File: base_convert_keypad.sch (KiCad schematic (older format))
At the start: 32 parts, among them SW10 B13, SW11 B2, SW12 B6, SW13 B10, SW14 B14, SW15 B3, SW16 B7, SW17 B11, SW18 B15, SW19 0, SW20 4, SW21 8, SW22 C, SW23 1, SW24 5, SW25 9, SW26 D, SW27 2, SW28 6, SW29 A, SW3 B0, SW30 E, SW31 3, SW32 7, SW33 B, SW34 F, SW4 B4, SW5 B8, SW6 B12, SW7 B1, SW8 B5, SW9 B9

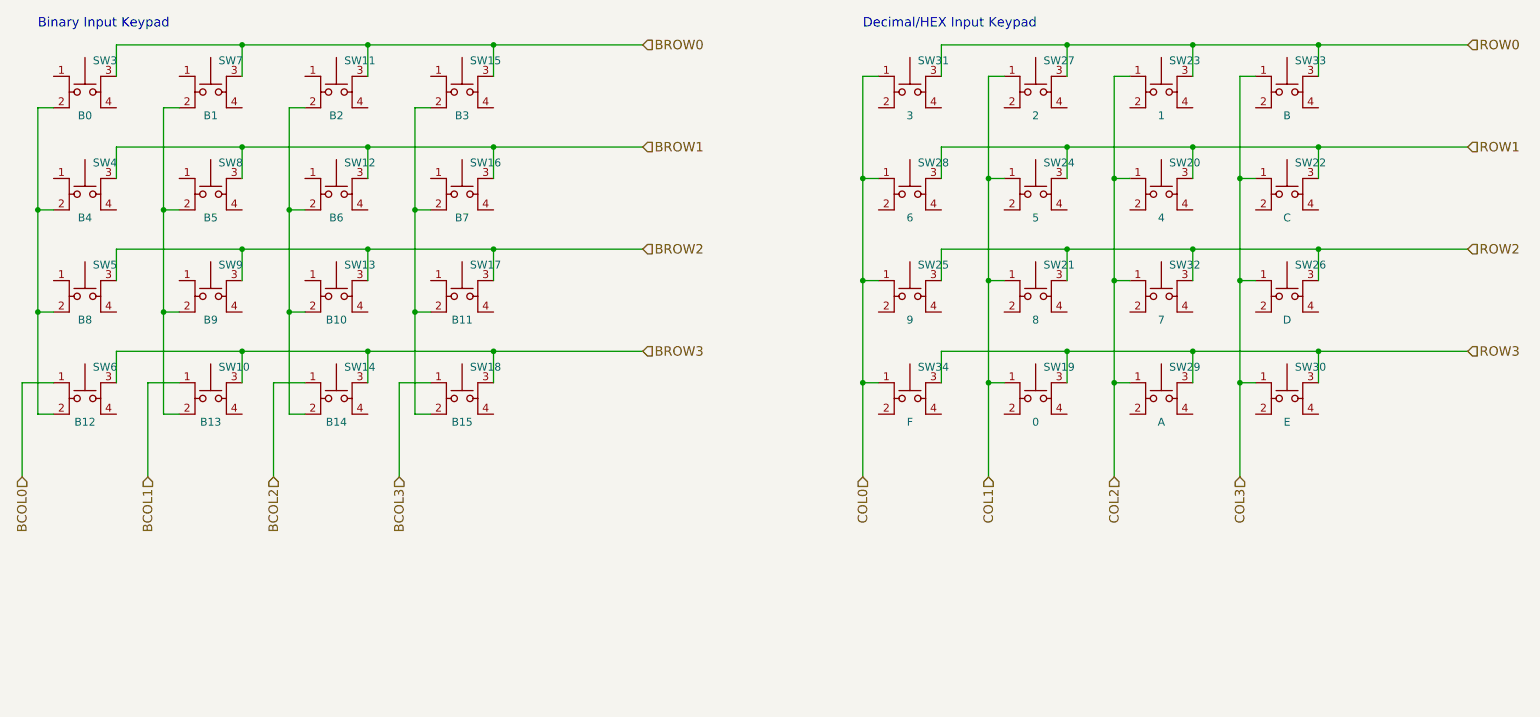
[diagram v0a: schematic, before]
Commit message: move clear button to keypad sheet
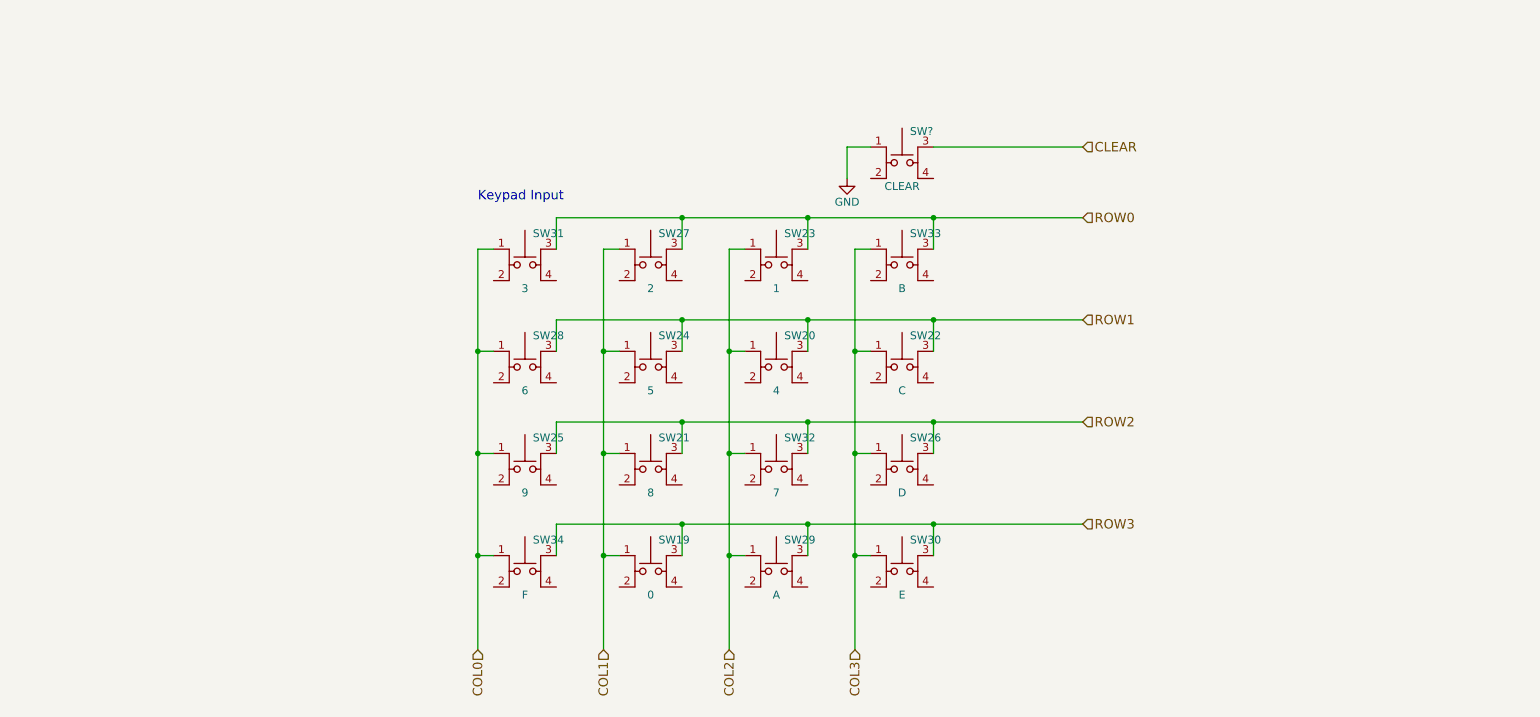
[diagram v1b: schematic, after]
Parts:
- removed SW10: B13, Buttons_Switches_THT:SW_TH_Tactile_Omron_B3F-10xx, symbol SW_Push_Dual2
- removed SW11: B2, Buttons_Switches_THT:SW_TH_Tactile_Omron_B3F-10xx, symbol SW_Push_Dual2
- removed SW12: B6, Buttons_Switches_THT:SW_TH_Tactile_Omron_B3F-10xx, symbol SW_Push_Dual2
- removed SW13: B10, Buttons_Switches_THT:SW_TH_Tactile_Omron_B3F-10xx, symbol SW_Push_Dual2
- removed SW14: B14, Buttons_Switches_THT:SW_TH_Tactile_Omron_B3F-10xx, symbol SW_Push_Dual2
- removed SW15: B3, Buttons_Switches_THT:SW_TH_Tactile_Omron_B3F-10xx, symbol SW_Push_Dual2
- removed SW16: B7, Buttons_Switches_THT:SW_TH_Tactile_Omron_B3F-10xx, symbol SW_Push_Dual2
- removed SW17: B11, Buttons_Switches_THT:SW_TH_Tactile_Omron_B3F-10xx, symbol SW_Push_Dual2
- removed SW18: B15, Buttons_Switches_THT:SW_TH_Tactile_Omron_B3F-10xx, symbol SW_Push_Dual2
- removed SW3: B0, Buttons_Switches_THT:SW_TH_Tactile_Omron_B3F-10xx, symbol SW_Push_Dual2
- removed SW4: B4, Buttons_Switches_THT:SW_TH_Tactile_Omron_B3F-10xx, symbol SW_Push_Dual2
- removed SW5: B8, Buttons_Switches_THT:SW_TH_Tactile_Omron_B3F-10xx, symbol SW_Push_Dual2
- removed SW6: B12, Buttons_Switches_THT:SW_TH_Tactile_Omron_B3F-10xx, symbol SW_Push_Dual2
- removed SW7: B1, Buttons_Switches_THT:SW_TH_Tactile_Omron_B3F-10xx, symbol SW_Push_Dual2
- removed SW8: B5, Buttons_Switches_THT:SW_TH_Tactile_Omron_B3F-10xx, symbol SW_Push_Dual2
- removed SW9: B9, Buttons_Switches_THT:SW_TH_Tactile_Omron_B3F-10xx, symbol SW_Push_Dual2
- added SW?: CLEAR, Buttons_Switches_THT:SW_TH_Tactile_Omron_B3F-10xx, symbol SW_Push_Dual2
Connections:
- new net CLEAR: SW?.3
- new net GND: SW?.1
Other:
- note added: "Keypad Input"
- note removed: "Binary Input Keypad"
- note removed: "Decimal/HEX Input Keypad"
- moved on the sheet: SW19, SW20, SW21, SW22, SW23, SW24, SW25, SW26, SW27, SW28, SW29, SW30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

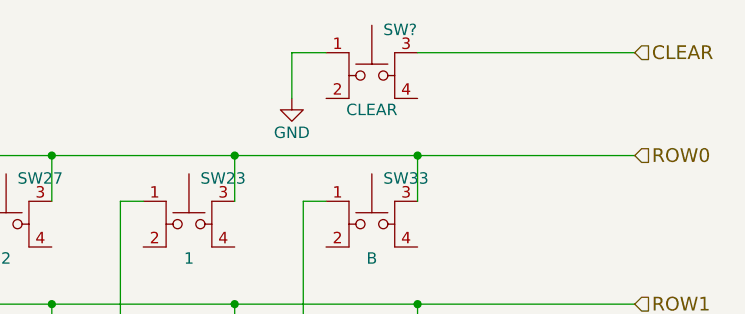
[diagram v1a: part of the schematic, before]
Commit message: update switch fields
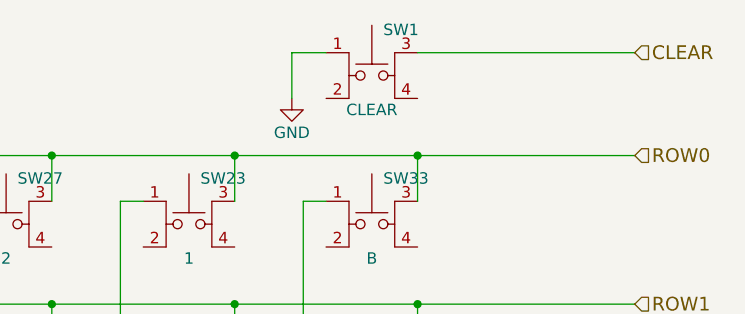
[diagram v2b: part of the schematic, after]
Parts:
- SW1: renamed from SW?; footprint Buttons_Switches_THT:SW_TH_Tactile_Omron_B3F-10xx -> (none); Description NONE -> SWITCH TACTILE SPST-NO 0.05A 12V; Manufacture NONE -> C&K; Mfg Part Number NONE -> PTS645SK95SMTR92LFS; Package NONE -> 6mm SMT
- SW19, SW20, SW21, SW22, SW23, SW24, SW25, SW26, SW27, SW28, SW29, SW30, SW31, SW32, SW33, SW34: Description NONE -> SWITCH TACTILE SPST-NO 0.05A 12V; Manufacture NONE -> C&K; Mfg Part Number NONE -> PTS645SK95SMTR92LFS; Package NONE -> 6mm SMT
